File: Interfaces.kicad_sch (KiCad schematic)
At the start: 6 parts, among them J6 282834-4, J7 200528-0100, U3 D5V0P4UR6SO, U7 D5V0P4UR6SO

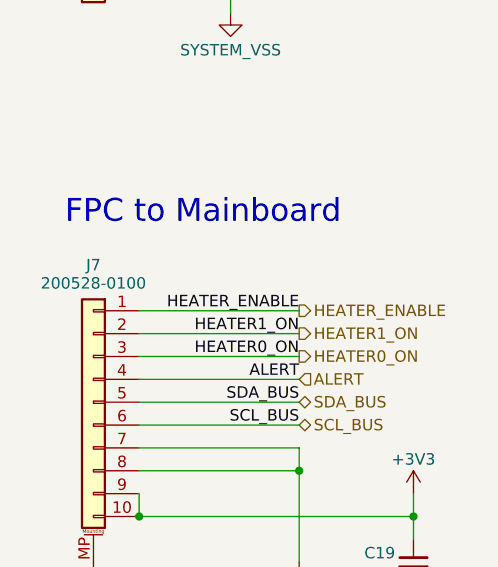
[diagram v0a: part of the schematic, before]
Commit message: Updated FPC connector
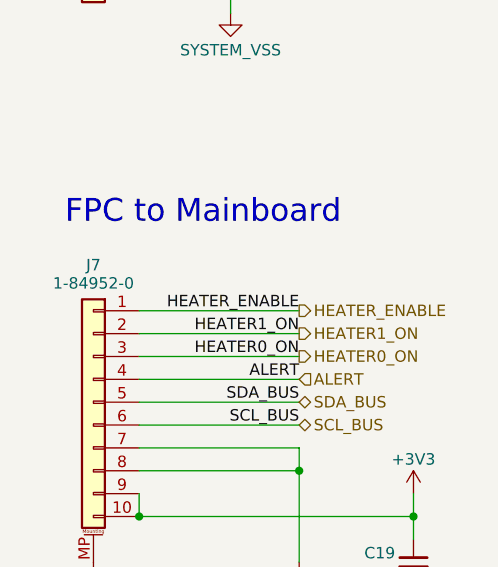
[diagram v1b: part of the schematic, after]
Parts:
- J7: value 200528-0100 -> 1-84952-0; footprint Connector_FFC-FPC:Molex_200528-0100_1x10-1MP_P1.00mm_Horizontal -> Connector_FFC-FPC:TE_1-84952-0_1x10-1MP_P1.0mm_Horizontal
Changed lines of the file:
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@@
 (kicad_sch
-	(version 20231120)
+	(version 20250114)
 	(generator "eeschema")
-	(generator_version "8.0")
+	(generator_version "9.0")
 	(paper "USLetter")
 	(title_block
@@
 		(comment 3 "V. Rajesh")
 	)
+	(text "FPC to Mainboard"
+		(exclude_from_sim no)
+		(at 99.822 88.138 0)
+		(effects
+			(font
+				(size 2.54 2.54)
+			)
+		)
+	)
+	(text "Power Connector"
+		(exclude_from_sim no)
+		(at 100.076 41.91 0)
+		(effects
+			(font
+				(size 2.54 2.54)
+			)
+		)
+	)
 	(junction
 		(at 123.19 121.92)
@@
 		)
 	)
-	(text "FPC to Mainboard"
-		(exclude_from_sim no)
-		(at 99.822 88.138 0)
-		(effects
-			(font
-				(size 2.54 2.54)
-			)
-		)
-	)
-	(text "Power Connector"
-		(exclude_from_sim no)
-		(at 100.076 41.91 0)
-		(effects
-			(font
-				(size 2.54 2.54)
-			)
-		)
-	)
 	(label "SDA_BUS"
 		(at 158.75 109.22 0)
-		(fields_autoplaced yes)
 		(effects
 			(font
@@
 	(label "SDA_BUS"
 		(at 110.49 109.22 180)
-		(fields_autoplaced yes)
 		(effects
 			(font
@@
 	(label "ALERT"
 		(at 110.49 106.68 180)
-		(fields_autoplaced yes)
 		(effects
 			(font
@@
 	(label "SCL_BUS"
 		(at 158.75 114.3 0)
-		(fields_autoplaced yes)
 		(effects
 			(font
@@
 	(label "HEATER0_ON"
 		(at 110.49 104.14 180)
-		(fields_autoplaced yes)
 		(effects
 			(font
@@
 	(label "HEATER1_ON"
 		(at 110.49 101.6 180)
-		(fields_autoplaced yes)
 		(effects
 			(font
@@
 	(label "HEATER1_ON"
 		(at 160.02 58.42 0)
-		(fields_autoplaced yes)
 		(effects
 			(font
@@
 	(label "HEATER0_ON"
 		(at 160.02 63.5 0)
-		(fields_autoplaced yes)
 		(effects
 			(font
@@
 	(label "HEATER_ENABLE"
 		(at 214.63 63.5 180)
-		(fields_autoplaced yes)
 		(effects
 			(font
@@
 	(label "ALERT"
 		(at 214.63 58.42 180)
-		(fields_autoplaced yes)
 		(effects
 			(font
@@
 	(label "SCL_BUS"
 		(at 110.49 111.76 180)
-		(fields_autoplaced yes)
 		(effects
 			(font
@@
 	(label "HEATER_ENABLE"
 		(at 110.49 99.06 180)
-		(fields_autoplaced yes)
 		(effects
 			(font
@@
 		(shape bidirectional)
 		(at 110.49 109.22 0)
-		(fields_autoplaced yes)
 		(effects
 			(font
@@
 		(shape bidirectional)
 		(at 110.49 111.76 0)
-		(fields_autoplaced yes)
 		(effects
 			(font
@@
 		(shape output)
 		(at 110.49 101.6 0)
-		(fields_autoplaced yes)
 		(effects
 			(font
@@
 		(shape output)
 		(at 110.49 99.06 0)
-		(fields_autoplaced yes)
 		(effects
 			(font
@@
 		(shape output)
 		(at 110.49 104.14 0)
-		(fields_autoplaced yes)
 		(effects
 			(font
@@
 		(shape input)
 		(at 110.49 106.68 0)
-		(fields_autoplaced yes)
 		(effects
 			(font
@@
 			)
 		)
-		(property "Value" "200528-0100"
+		(property "Value" "1-84952-0"
 			(at 87.63 96.012 0)
 			(effects
@@
 			)
 		)
-		(property "Footprint" "Connector_FFC-FPC:Molex_200528-0100_1x10-1MP_P1.00mm_Horizontal"
+		(property "Footprint" "Connector_FFC-FPC:TE_1-84952-0_1x10-1MP_P1.0mm_Horizontal"
 			(at 87.63 109.22 0)
 			(effects

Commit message: v3.1 Updates
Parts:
- added J6: 205338-0002, Connector_Molex:Molex_Pico-Lock_205338-0002_1x02-1MP_P2.00mm_Horizontal, symbol Connector_Generic_MountingPin:Conn_01x02_MountingPin
- added J7: 205338-0004, Connector_Molex:Molex_Pico-Lock_205338-0004_1x04-1MP_P2.00mm_Horizontal, symbol Connector_Generic_MountingPin:Conn_01x04_MountingPin
- C14: renamed from C19; value 10uF -> 10u
- D6: renamed from D5; value 10V -> SMAJ9.0AHR3G; Part SMAJ9.0AHR3G -> 10V
- J9: renamed from J7; value 1-84952-0 -> 522711069; footprint Connector_FFC-FPC:TE_1-84952-0_1x10-1MP_P1.0mm_Horizontal -> Argus-Connectors:CON_522711069_MOL
- renumbered J6 to J8, U3 to U6
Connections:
- net GND: now also J6.MP (MountPin), J7.MP (MountPin)
- net SYSTEM_VDD: now also J6.1 (Pin_1), J7.3 (Pin_3), J7.4 (Pin_4)
- net SYSTEM_VSS: now also J6.2 (Pin_2), J7.1 (Pin_1), J7.2 (Pin_2)
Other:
- note added: "Power Connectors"
- note removed: "Power Connector"
- moved on the sheet: D6, J8

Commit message: Idk some changes
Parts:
- C14: MPN (none) -> C386084
- J7: MPN (none) -> C916325
- J8: now not fitted; now left out of the parts list
- J9: MPN (none) -> C588180
- U6, U7: MPN (none) -> C531179
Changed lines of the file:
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@@
+			)
+		)
+		(property "MPN" "C916325"
+			(at 80.01 60.96 0)
+			(effects
+				(font
+					(size 1.27 1.27)
+				)
+				(hide yes)
 			)
 		)
@@
 			)
 		)
+		(property "MPN" "C531179"
+			(at 186.69 111.76 0)
+			(effects
+				(font
+					(size 1.27 1.27)
+				)
+				(hide yes)
+			)
+		)
 		(pin "6"
 		)
@@
 			)
 		)
+		(property "MPN" "C531179"
+			(at 186.69 60.96 0)
+			(effects
+				(font
+					(size 1.27 1.27)
+				)
+				(hide yes)
+			)
+		)
 		(pin "6"
 		)
@@
 		(unit 1)
 		(exclude_from_sim no)
-		(in_bom yes)
-		(on_board yes)
-		(dnp no)
+		(in_bom no)
+		(on_board yes)
+		(dnp yes)
 		(property "Reference" "J8"
 			(at 106.68 53.086 0)
@@
 			)
 		)
+		(property "MPN" "C588180"
+			(at 87.63 109.22 0)
+			(effects
+				(font
+					(size 1.27 1.27)
+				)
+				(hide yes)
+			)
+		)
 		(pin "1"
 		)
@@
 			(at 123.19 127 0)
 			(effects
+				(font
+					(size 1.27 1.27)
+				)
+				(hide yes)
+			)
+		)
+		(property "MPN" "C386084"
+			(at 123.19 127 0)
+			(effects
